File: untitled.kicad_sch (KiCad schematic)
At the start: 66 parts, among them J3 V_bat_in, J4 V_bat_out, J5 Conn_01x05_Pin, J6 Conn_01x05_Pin, J7 Conn_01x05_Pin, U3 MCP6022, U4 ACPL-C87A

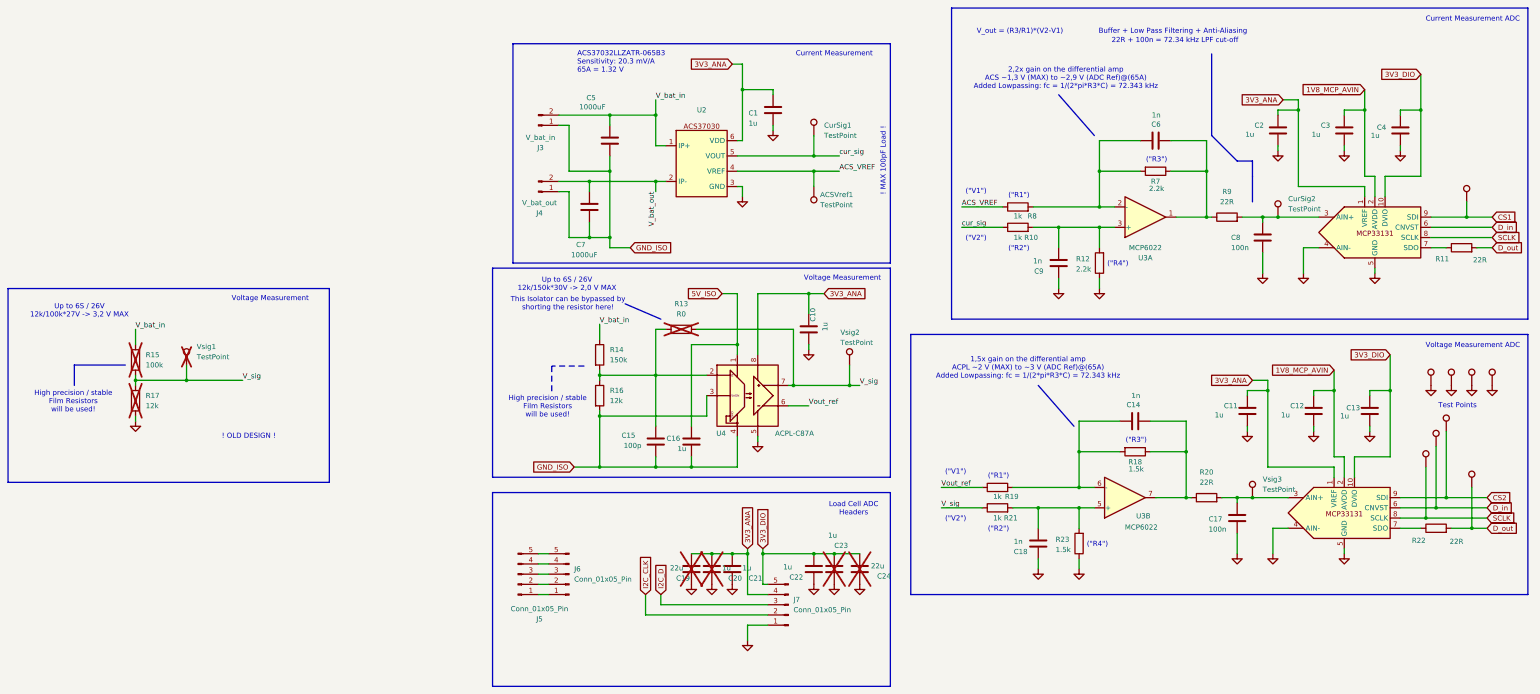
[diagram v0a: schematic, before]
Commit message: Improved layout, added TVS diodes. Rotated ESP32, Changed proper SPI pins, finalized the load cell module area.
[KiCad Version: 9.0.8]
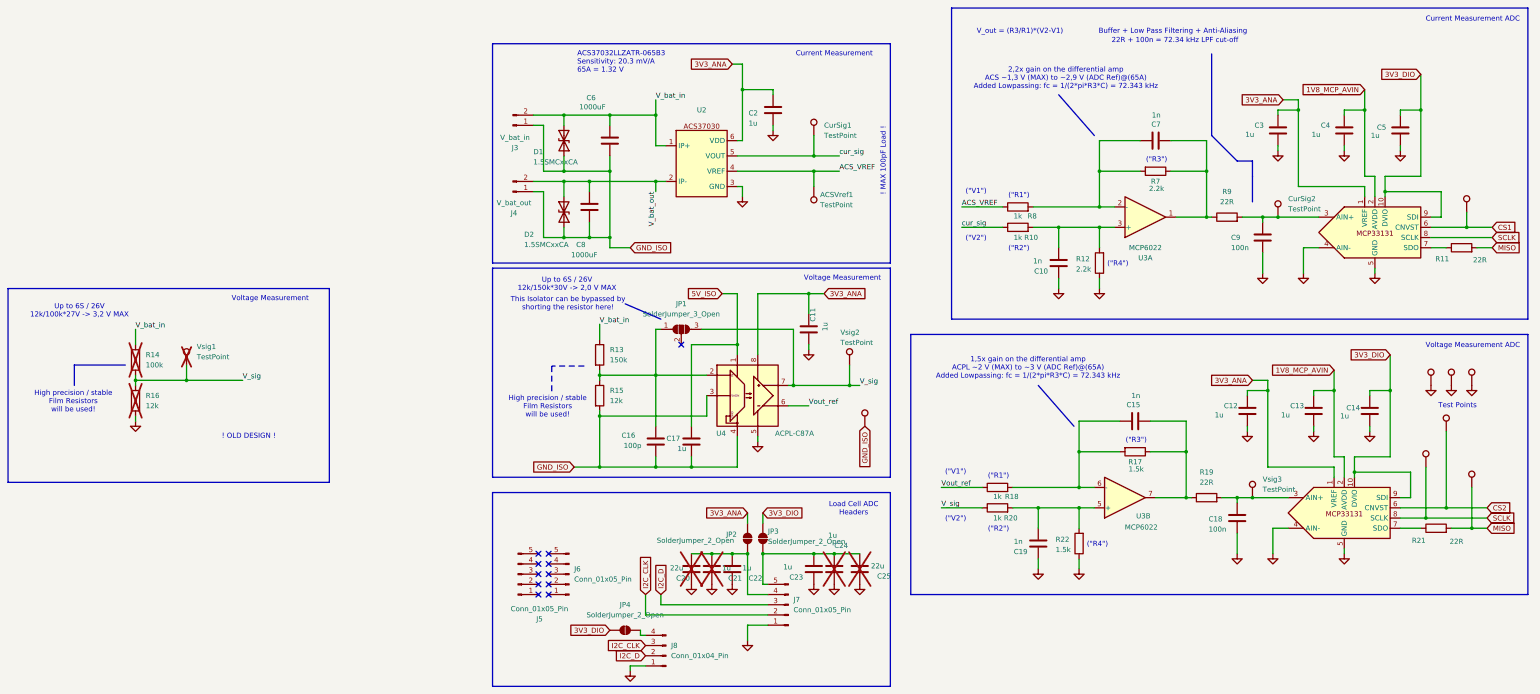
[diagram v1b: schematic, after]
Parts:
- removed Din1: TestPoint, TestPoint:TestPoint_Pad_D1.0mm, symbol Connector:TestPoint
- removed R13: R0, Resistor_SMD:R_0603_1608Metric_Pad0.98x0.95mm_HandSolder, symbol Device:R
- added D1, D2: 1.5SMCxxCA, Diode_SMD:D_SMC, symbol Diode:1.5SMCxxCA
- added J8: Conn_01x04_Pin, Connector_PinHeader_2.54mm:PinHeader_1x04_P2.54mm_Vertical, symbol Connector:Conn_01x04_Pin
- added JP1: SolderJumper_3_Open, Jumper:SolderJumper-3_P1.3mm_Open_RoundedPad1.0x1.5mm, symbol Jumper:SolderJumper_3_Open
- added JP2, JP3, JP4: SolderJumper_2_Open, Jumper:SolderJumper-2_P1.3mm_Open_RoundedPad1.0x1.5mm, symbol Jumper:SolderJumper_2_Open
- J3, J4: footprint Connector_AMASS:AMASS_XT60PW-M_1x02_P7.20mm_Horizontal -> custom_footprints:AMASS_XT60PW-M_1x02_P7.20mm_Horizontal_with3DModel
- U2: footprint custom_footprints:SOIC-6 -> custom_footprints:ACS37030LLZATR-065B3
- renumbered C9 to C10, C10 to C11, C11 to C12, C12 to C13, C13 to C14, C14 to C15, C15 to C16, C16 to C17, C17 to C18, C18 to C19, C1 to C2, C19 to C20, C20 to C21, C21 to C22, C22 to C23, C23 to C24, C24 to C25, C2 to C3, C3 to C4, C4 to C5, C5 to C6, C6 to C7, C7 to C8, C8 to C9, R14 to R13, R15 to R14, R16 to R15, R17 to R16, R18 to R17, R19 to R18, R20 to R19, R21 to R20, R22 to R21, R23 to R22
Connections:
- net 3V3_ANA: now also JP2.2 (B); no longer C20.2, C21.2, C22.2, J7.4 (Pin_4)
- net 3V3_DIO: now also MCP1.9 (SDI), MCP2.9 (SDI), JP3.2 (B), JP4.1 (A); no longer C23.2, C24.2, C25.2, J7.5 (Pin_5)
- net CS1: now also MCP1.6 (CNVST); no longer MCP1.9 (SDI)
- net CS2: now also MCP2.6 (CNVST); no longer MCP2.9 (SDI)
- net GND: now also J8.1 (Pin_1); no longer GND4.1
- net GND_ISO: now also GND4.1, D1.1 (A1), D2.1 (A1)
- net I2C_CLK: now also J8.3 (Pin_3)
- net I2C_D: now also J8.2 (Pin_2)
- net V_bat_in: now also D1.2 (A2)
- net V_bat_out: now also D2.2 (A2)
- net V_sig: now also JP1.3 (B)
- net at C16.1, R13.2, R15.1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: now also JP1.1 (A)
- net at J6.1 (Pin_1): no longer J5.1 (Pin_1)
- net at J6.2 (Pin_2): no longer J5.2 (Pin_2)
- net at J6.3 (Pin_3): no longer J5.3 (Pin_3)
- net at J6.4 (Pin_4): no longer J5.4 (Pin_4)
- net at J6.5 (Pin_5): no longer J5.5 (Pin_5)
- removed net D_in: MCP1.6 (CNVST), MCP2.6 (CNVST)
- net D_out renamed MISO
- new net: C23.2, C24.2, C25.2, J7.5 (Pin_5), JP3.1 (A)
- new net: C20.2, C21.2, C22.2, J7.4 (Pin_4), JP2.1 (A)
- new net: J8.4 (Pin_4), JP4.2 (B)
- no-connect marks 0 -> 11
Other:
- moved on the sheet: J3, J4

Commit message: Improved layout.
[KiCad Version: 9.0.8]
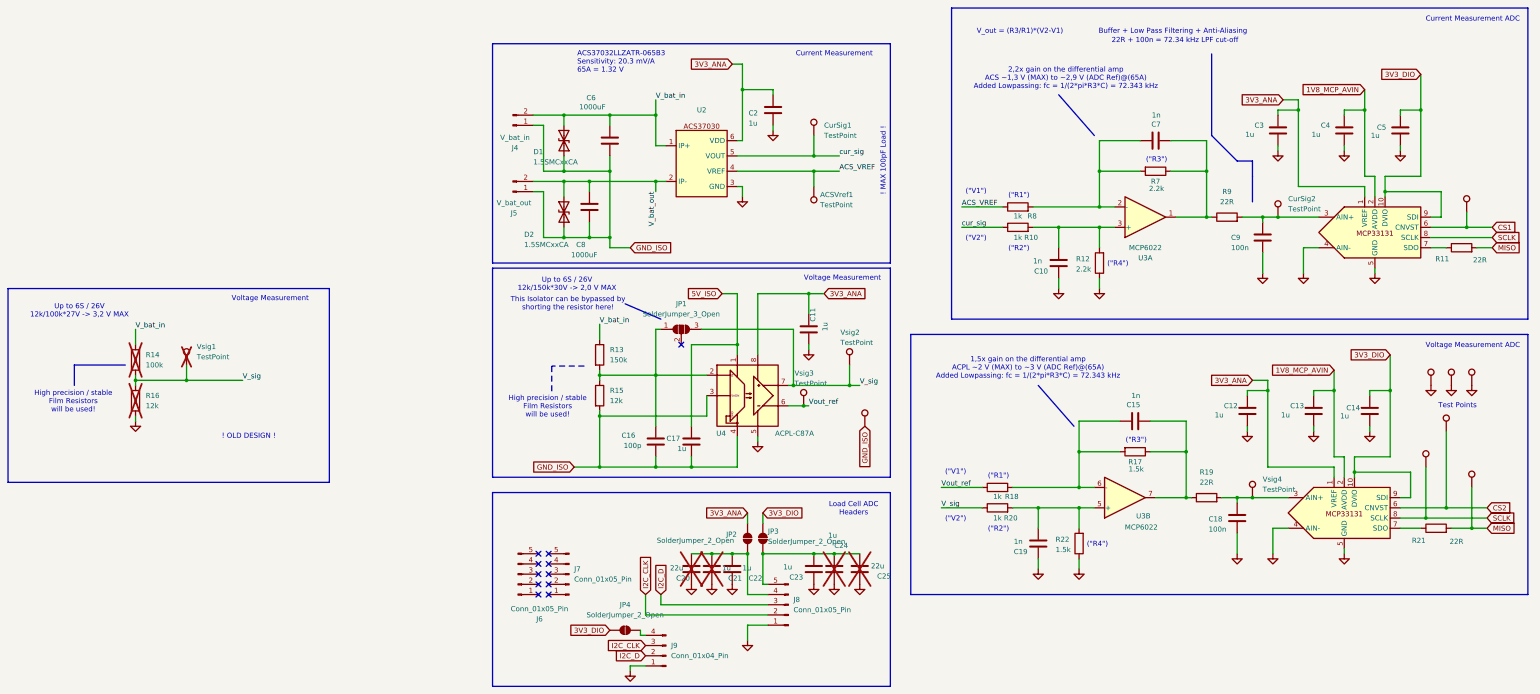
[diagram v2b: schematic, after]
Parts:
- added Vsig3: TestPoint, TestPoint:TestPoint_Pad_D1.0mm, symbol Connector:TestPoint
- renumbered J3 to J4, J4 to J5, J5 to J6, J6 to J7, J7 to J8, J8 to J9, Vsig3 to Vsig4
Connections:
- net Vout_ref: now also Vsig3.1
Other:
- company: Torakka Design Oy -> (none)
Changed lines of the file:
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@@
 		(title "Measurements")
 		(rev "1.0")
-		(company "Torakka Design Oy")
 	)
 	(rectangle
@@
 	)
 	(junction
+		(at 99.06 115.57)
+		(diameter 0)
+		(color 0 0 0 0)
+	)
+	(junction
 		(at 231.14 111.76)
 		(diameter 0)
@@
 	(wire
 		(pts
+			(xy 99.06 115.57) (xy 100.33 115.57)
+		)
+		(stroke
+			(width 0)
+			(type default)
+		)
+	)
+	(wire
+		(pts
 			(xy 50.8 43.18) (xy 50.8 45.72)
 		)
@@
 	(wire
 		(pts
-			(xy 95.25 115.57) (xy 100.33 115.57)
+			(xy 95.25 115.57) (xy 99.06 115.57)
 		)
 		(stroke
@@
 		(dnp no)
 		(fields_autoplaced yes)
-		(property "Reference" "Vsig3"
+		(property "Reference" "Vsig4"
 			(at 213.36 133.8579 0)
 			(effects
@@
 			(project "motor_testbench_v1_0"
 				(path "/da638649-102c-44f9-b928-e91cd399cc2f/2da1fd24-7545-4e4a-b589-72e0f66a31f4"
-					(reference "Vsig3")
+					(reference "Vsig4")
 					(unit 1)
 				)
@@
 		(dnp no)
 		(fields_autoplaced yes)
-		(property "Reference" "J7"
+		(property "Reference" "J8"
 			(at 96.52 163.8299 0)
 			(effects
@@
 			(project "motor_testbench_v1_0"
 				(path "/da638649-102c-44f9-b928-e91cd399cc2f/2da1fd24-7545-4e4a-b589-72e0f66a31f4"
-					(reference "J7")
+					(reference "J8")
 					(unit 1)
 				)
@@
 	)
 	(symbol
+		(lib_id "Connector:TestPoint")
+		(at 99.06 115.57 0)
+		(unit 1)
+		(exclude_from_sim no)
+		(in_bom yes)
+		(on_board yes)
+		(dnp no)
+		(property "Reference" "Vsig3"
+			(at 96.774 107.442 0)
+			(effects
+				(font
+					(size 1.27 1.27)
+				)
+				(justify left)
+			)
+		)
+		(property "Value" "TestPoint"
+			(at 96.774 109.982 0)
+			(effects
+				(font
+					(size 1.27 1.27)
+				)
+				(justify left)
+			)
+		)
+		(property "Footprint" "TestPoint:TestPoint_Pad_D1.0mm"
+			(at 104.14 115.57 0)
+			(effects
+				(font
+					(size 1.27 1.27)
+				)
+				(hide yes)
+			)
+		)
+		(property "Datasheet" "~"
+			(at 104.14 115.57 0)
+			(effects
+				(font
+					(size 1.27 1.27)
+				)
+				(hide yes)
+			)
+		)
+		(property "Description" "test point"
+			(at 99.06 115.57 0)
+			(effects
+				(font
+					(size 1.27 1.27)
+				)
+				(hide yes)
+			)
+		)
+		(pin "1"
+		)
+		(instances
+			(project "motor_testbench_v1_0"
+				(path "/da638649-102c-44f9-b928-e91cd399cc2f/2da1fd24-7545-4e4a-b589-72e0f66a31f4"
+					(reference "Vsig3")
+					(unit 1)
+				)
+			)
+		)
+	)
+	(symbol
 		(lib_id "Device:R")
 		(at -67.31 104.14 0)
@@
 		(dnp no)
 		(fields_autoplaced yes)
-		(property "Reference" "J6"
+		(property "Reference" "J7"
 			(at 41.91 156.2099 0)
 			(effects
@@
 			(project "motor_testbench_v1_0"
 				(path "/da638649-102c-44f9-b928-e91cd399cc2f/2da1fd24-7545-4e4a-b589-72e0f66a31f4"
-					(reference "J6")
+					(reference "J7")
 					(unit 1)
 				)
@@
 		(on_board yes)
 		(dnp no)
-		(property "Reference" "J4"
+		(property "Reference" "J5"
 			(at 26.924 67.564 0)
 			(effects
@@
 			(project "motor_testbench_v1_0"
 				(path "/da638649-102c-44f9-b928-e91cd399cc2f/2da1fd24-7545-4e4a-b589-72e0f66a31f4"
-					(reference "J4")
+					(reference "J5")
 					(unit 1)
 				)
@@
 		(on_board yes)
 		(dnp no)
-		(property "Reference" "J5"
+		(property "Reference" "J6"
 			(at 33.274 168.656 0)
 			(effects
@@
 			(project "motor_testbench_v1_0"
 				(path "/da638649-102c-44f9-b928-e91cd399cc2f/2da1fd24-7545-4e4a-b589-72e0f66a31f4"
-					(reference "J5")
+					(reference "J6")
 					(unit 1)
 				)
@@
 		(on_board yes)
 		(dnp no)
-		(property "Reference" "J3"
+		(property "Reference" "J4"
 			(at 27.178 51.308 0)
 			(effects
@@
 			(project "motor_testbench_v1_0"
 				(path "/da638649-102c-44f9-b928-e91cd399cc2f/2da1fd24-7545-4e4a-b589-72e0f66a31f4"
-					(reference "J3")
+					(reference "J4")
 					(unit 1)
 				)
@@
 		(dnp no)
 		(fields_autoplaced yes)
-		(property "Reference" "J8"
+		(property "Reference" "J9"
 			(at 66.04 175.2599 0)
 			(effects
@@
 			(project "motor_testbench_v1_0"
 				(path "/da638649-102c-44f9-b928-e91cd399cc2f/2da1fd24-7545-4e4a-b589-72e0f66a31f4"
-					(reference "J8")
+					(reference "J9")
 					(unit 1)
 				)

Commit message: testi
[KiCad Version: 9.0.7]
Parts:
- removed R14: 100k, Resistor_SMD:R_0603_1608Metric_Pad0.98x0.95mm_HandSolder, symbol Device:R
- removed R16: 12k, Resistor_SMD:R_0603_1608Metric_Pad0.98x0.95mm_HandSolder, symbol Device:R
- removed Vsig1: TestPoint, TestPoint:TestPoint_Pad_D1.0mm, symbol Connector:TestPoint
- ACSVref1, CurSig1, CurSig2, Dout1, SCLK1, Vsig2: now left out of the parts list
- C10: renamed from C11; value 1u -> 1uF; Manufacturer_Part_Number (none) -> CL10B105KB8NQNC
- C11: renamed from C23; value 1u -> 1uF; Manufacturer_Part_Number (none) -> CL10B105KB8NQNC
- C12: renamed from C24; value 1u -> 1uF
- C13: renamed from C25; value 22u -> 22uF
- C14: renamed from C19; value 1n -> 1nF
- C15: renamed from C10; value 1n -> 1nF
- C16: renamed from C15; value 1n -> 1nF
- C17: renamed from C7; value 1n -> 1nF
- C18: value 100n -> 100nF
- C19: renamed from C12; value 1u -> 1uF; Manufacturer_Part_Number (none) -> CL10B105KB8NQNC
- C20: renamed from C9; value 100n -> 100nF
- C21: renamed from C3; value 1u -> 1uF; Manufacturer_Part_Number (none) -> CL10B105KB8NQNC
- C22: renamed from C13; value 1u -> 1uF; Manufacturer_Part_Number (none) -> CL10B105KB8NQNC
- C23: renamed from C4; value 1u -> 1uF; Manufacturer_Part_Number (none) -> CL10B105KB8NQNC
- C24: renamed from C14; value 1u -> 1uF; Manufacturer_Part_Number (none) -> CL10B105KB8NQNC
- C25: renamed from C5; value 1u -> 1uF; Manufacturer_Part_Number (none) -> CL10B105KB8NQNC
- C4: renamed from C16; value 100p -> 100pF
- C5: renamed from C17; value 1u -> 1uF; Manufacturer_Part_Number (none) -> CL10B105KB8NQNC
- C6: renamed from C20; value 22u -> 22uF; now left out of the parts list
- C7: renamed from C21; value 1u -> 1uF
- C8: renamed from C22; value 1u -> 1uF; Manufacturer_Part_Number (none) -> CL10B105KB8NQNC
- C9: renamed from C2; value 1u -> 1uF; Manufacturer_Part_Number (none) -> CL10B105KB8NQNC
- CS1: renamed from CS2; now left out of the parts list
- CS2: renamed from CS1; now left out of the parts list
- GND1: renamed from GND4; now left out of the parts list
- GND2: renamed from GND1; now left out of the parts list
- GND3: renamed from GND2; now left out of the parts list
- GND4: renamed from GND3; now left out of the parts list
- Vsig1: renamed from Vsig3; now left out of the parts list
- Vsig3: renamed from Vsig4; now left out of the parts list
- renumbered C8 to C2, C6 to C3, J9 to J8, J8 to J9, JP4 to JP1, JP1 to JP2, JP2 to JP3, JP3 to JP4, R8 to R10, R10 to R11, R22 to R12, R12 to R13, R17 to R14, R7 to R15, R19 to R16, R9 to R17, R21 to R18, R11 to R19, R13 to R6, R15 to R7, R18 to R8, R20 to R9, U4 to U3, U3 to U4, MCP2 to U5, MCP1 to U6
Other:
- note removed: "! OLD DESIGN !"
- note removed: "Up to 6S / 26V 12k/100k*27V -> 3,2 V MAX"
